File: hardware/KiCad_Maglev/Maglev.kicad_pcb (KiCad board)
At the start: 4 copper layers, 265 x 130 mm, 114 parts, among them IC1 TLV1117LV33DCYR, J1 USB_C_Receptacle, J11 690367190672, J12 690367190672, J2 691103110002, J3 61300621121, J4 61300821121, J6 61300621121, J7 690367191672, J8 690367191672, U1 WE-TVS-82400102, U2 ESP32-C3, U4 TMAG5173A2QDBVRQ1, U5 TPS259474ARPWR, Y1 IQXC-42_830108213209

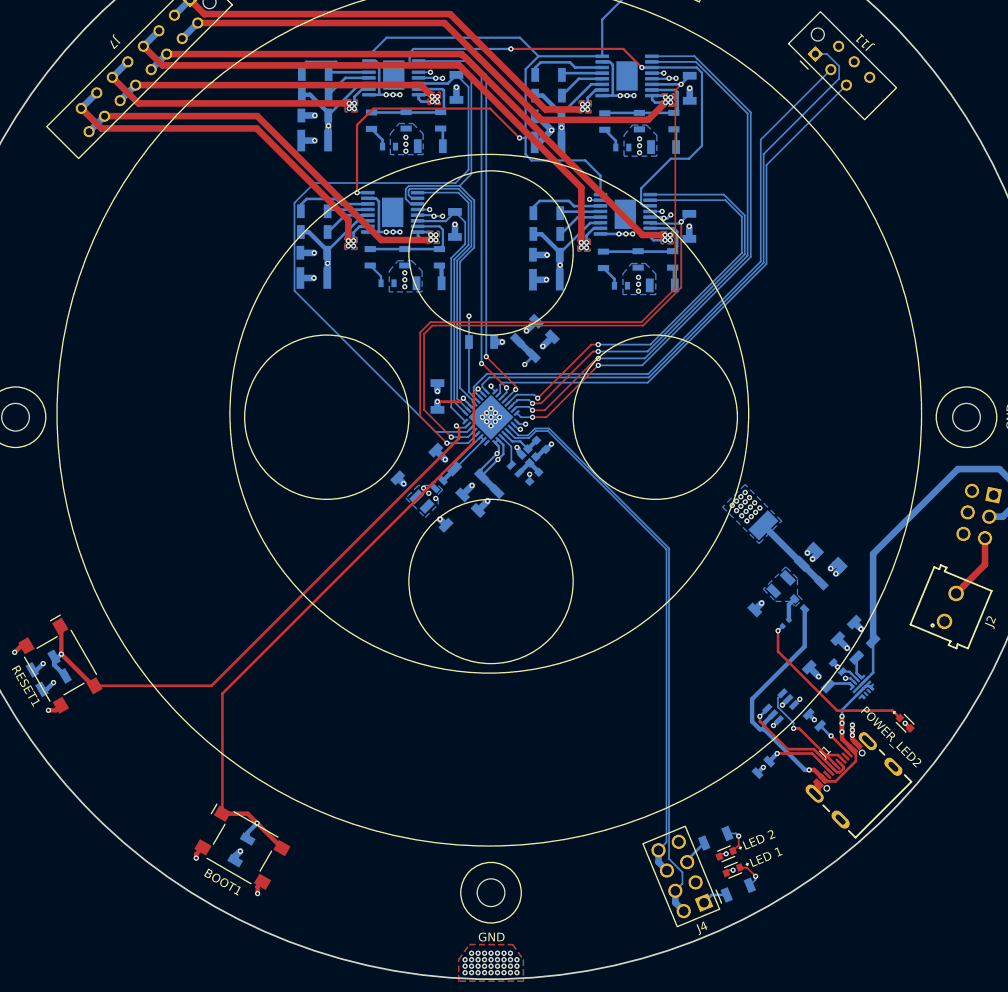
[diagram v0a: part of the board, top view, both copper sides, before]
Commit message: added test points in schematic
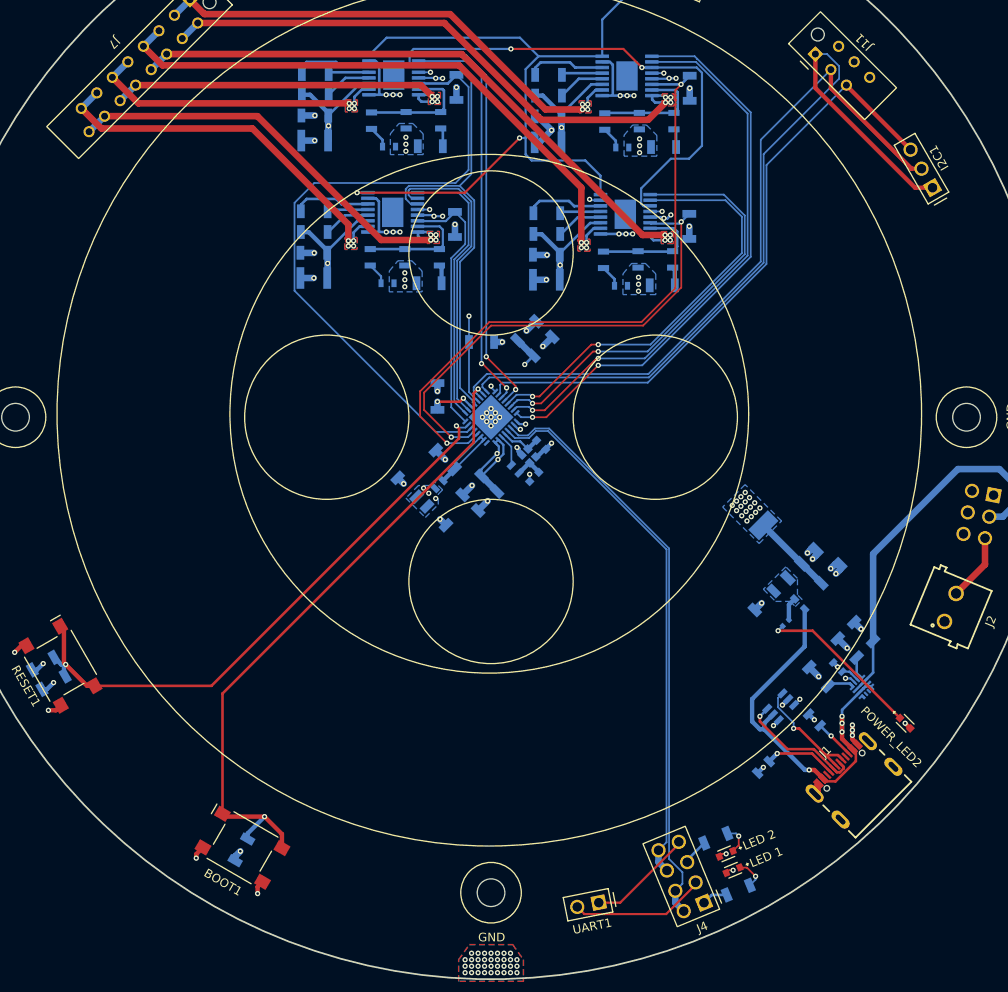
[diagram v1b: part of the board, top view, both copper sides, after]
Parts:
- added I2C1: 61300311121, Connector_THT_Wurth:J_Wurth_WR-PHD_61300311121, F.Cu at (266.1, 73.4)
- added UART1: 61300211121, Connector_THT_Wurth:J_Wurth_WR-PHD_61300211121, F.Cu at (227.5, 156.1)
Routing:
- net /I2C_SCL: track 133.0 -> 155.3 mm
- net /I2C_SDA: track 127.4 -> 143.9 mm
- net /RXD: track 0.00 -> 15.7 mm
- net /TXD: track 0.00 -> 12.3 mm
- net /I2C_INT: track 124.9 -> 135.5 mm
- net /Electromagnet Driver/PMODE: track 95.8 -> 88.4 mm
- net /HBRIDGE_A_ISENSE: track 78.5 -> 74.6 mm
- net /HBRIDGE_B_ISENSE: track 60.9 -> 56.9 mm
- net /USB_D+: track 50.3 -> 47.2 mm
- net /BOOT: track 73.1 -> 75.2 mm
- net /USB_D-: track 50.1 -> 48.3 mm
- net Net-(POWER_LED2-+): track 20.5 -> 19.1 mm

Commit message: Differential Pair USB
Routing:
- net Net-(J1-D+-PadA6): track 13.9 -> 15.2 mm
- net /USB_D+: track 47.2 -> 47.8 mm

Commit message: Add breakaway PCB bridge and QR code copper artwork
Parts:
- removed Magnet2: ~, CUSTOM:MagnetRing_2
- removed the REF** at (215.0, 119.0)
- removed REF**2: Electromagnet_2, CUSTOM:Electromagnet_2
- added 1: , , F.Cu at (145.4, 95.7)
- added 11: , , F.Cu at (145.4, 104.4)
- added 12: , , F.Cu at (145.3, 105.3)
- added 3: , , F.Cu at (145.5, 97.5)
- added 4: , , F.Cu at (145.5, 98.3)
- added 6: , , F.Cu at (145.5, 100.1)
- added 7: , , F.Cu at (145.5, 100.9)
- added 9: , , F.Cu at (145.4, 102.7)
- added ?: , , F.Cu at (145.3, 94.9)
- added REF**: BreakLine_1h_D0.5mm_P0.85mm, Panelization:BreakLine_1h_D0.5mm_P0.85mm, F.Cu at (149.7, 94.9)
- added REF**11: BreakLine_1h_D0.5mm_P0.85mm, Panelization:BreakLine_1h_D0.5mm_P0.85mm, F.Cu at (149.6, 104.4)
- added REF**12: BreakLine_1h_D0.5mm_P0.85mm, Panelization:BreakLine_1h_D0.5mm_P0.85mm, F.Cu at (149.7, 105.3)
- added REF**4: BreakLine_1h_D0.5mm_P0.85mm, Panelization:BreakLine_1h_D0.5mm_P0.85mm, F.Cu at (149.5, 98.3)
- added REF**6: BreakLine_1h_D0.5mm_P0.85mm, Panelization:BreakLine_1h_D0.5mm_P0.85mm, F.Cu at (149.5, 100.1)
- added REF**7: BreakLine_1h_D0.5mm_P0.85mm, Panelization:BreakLine_1h_D0.5mm_P0.85mm, F.Cu at (149.5, 100.9)
- added REF**9: BreakLine_1h_D0.5mm_P0.85mm, Panelization:BreakLine_1h_D0.5mm_P0.85mm, F.Cu at (149.6, 102.7)
- REF**1, REF**3: value Electromagnet_2 -> BreakLine_1h_D0.5mm_P0.85mm; footprint CUSTOM:Electromagnet_2 -> Panelization:BreakLine_1h_D0.5mm_P0.85mm
- moved REF**3 84.5 mm to (149.5, 97.5)
- moved REF**1 46.6 mm to (149.6, 95.7)
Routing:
- net /I2C_SCL: track 155.3 -> 355.2 mm, vias 1 -> 2
- net /I2C_INT: track 135.5 -> 334.4 mm
- net /I2C_SDA: track 143.9 -> 341.6 mm, vias 1 -> 2
- net /EM_B_N: track 122.8 -> 266.5 mm
- net /EM_A_P: track 121.4 -> 264.0 mm
- net /EM_B_P: track 134.5 -> 273.2 mm
- net /EM_C_N: track 99.6 -> 234.2 mm
- net /EM_A_N: track 112.0 -> 245.2 mm
- net /EM_C_P: track 117.5 -> 244.1 mm
- net /EM_D_P: track 146.9 -> 264.0 mm
- net /EM_D_N: track 127.9 -> 239.6 mm
- net /BOOT: track 75.2 -> 72.2 mm
- net GND: track 102.1 -> 102.5 mm, vias 355 -> 287
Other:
- outline, holes or cut-outs redrawn
